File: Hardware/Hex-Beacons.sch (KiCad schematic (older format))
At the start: 0 parts

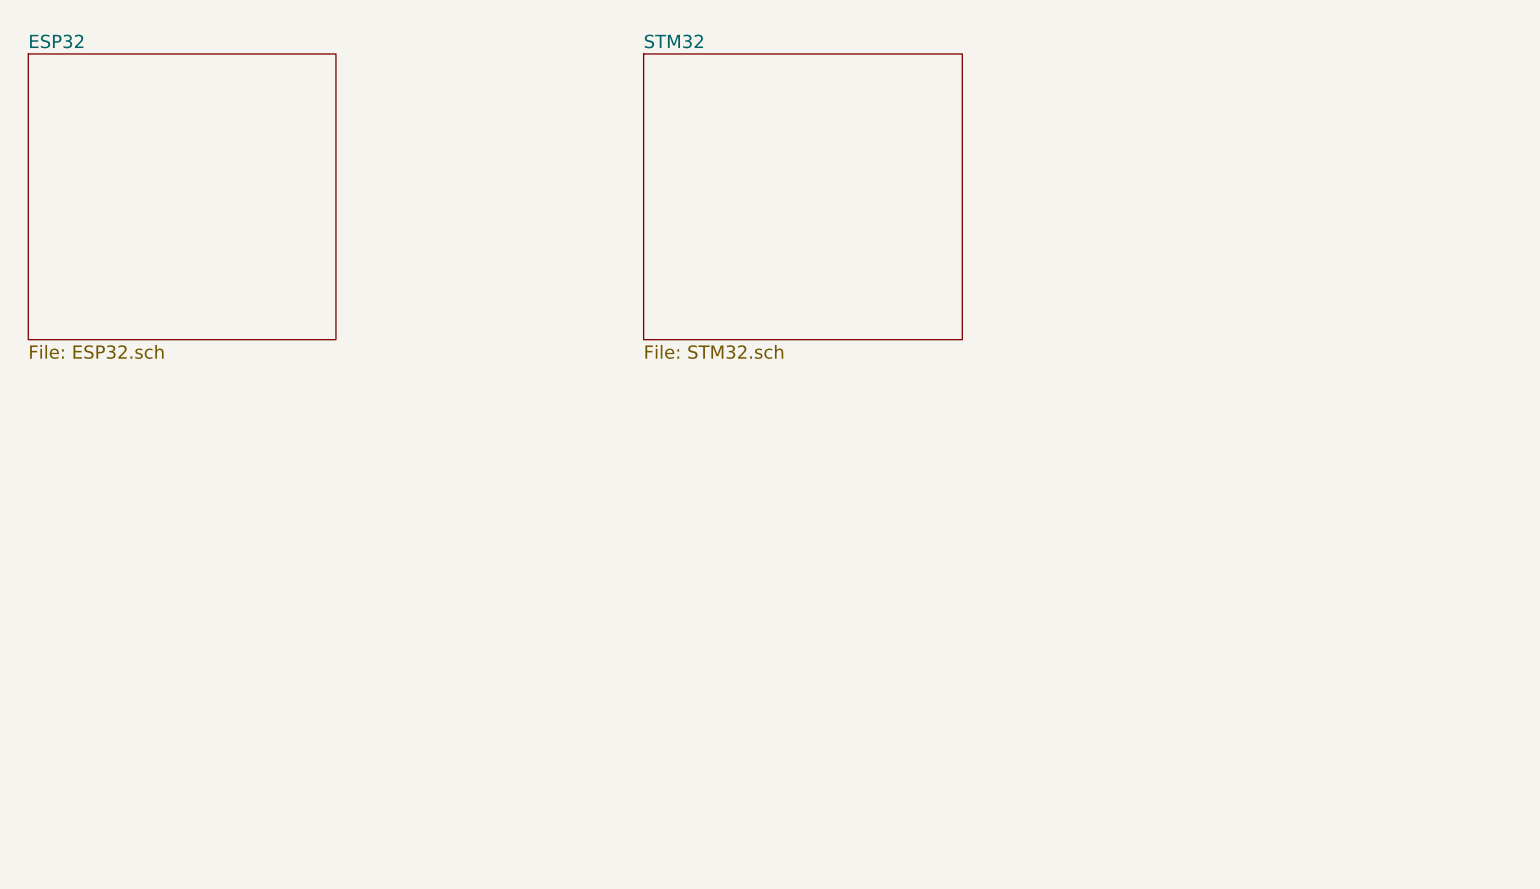
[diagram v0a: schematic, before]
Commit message: Base ESP32 sheet done. STM32 in place
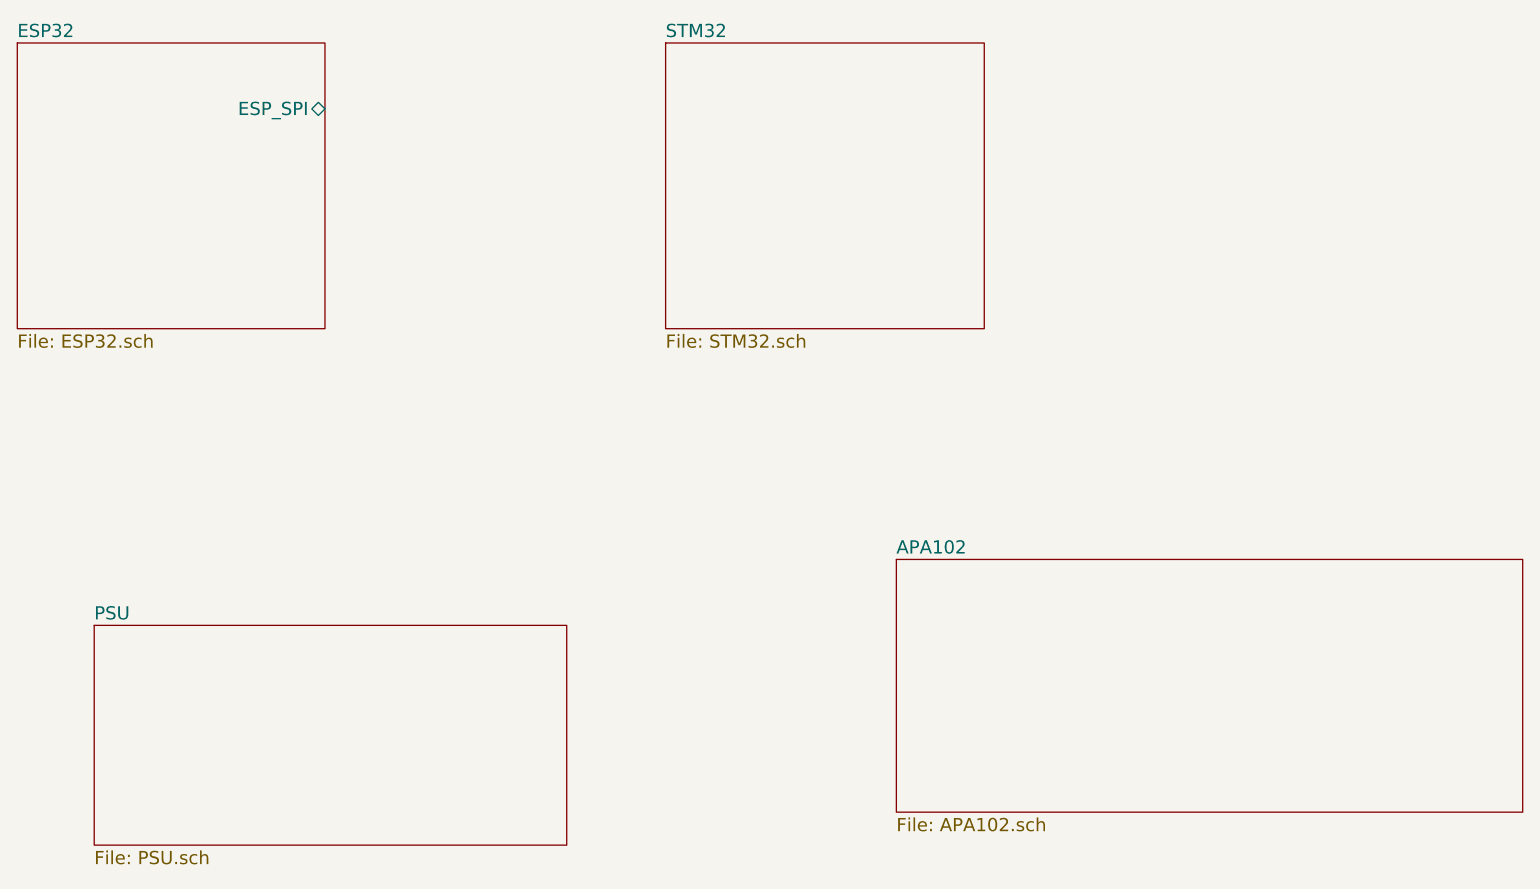
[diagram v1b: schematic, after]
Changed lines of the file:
@@
 LIBS:contrib
 LIBS:valves
-LIBS:crumpschemes
-LIBS:ESP32-footprints-Shem-Lib
-LIBS:espressif-xess
-LIBS:74xgxx
-LIBS:ac-dc
-LIBS:actel
-LIBS:allegro
-LIBS:Altera
-LIBS:analog_devices
-LIBS:battery_management
-LIBS:bbd
-LIBS:bosch
-LIBS:brooktre
-LIBS:cmos_ieee
-LIBS:dc-dc
-LIBS:diode
-LIBS:elec-unifil
-LIBS:ESD_Protection
-LIBS:ftdi
-LIBS:gennum
-LIBS:graphic
-LIBS:hc11
-LIBS:ir
-LIBS:Lattice
-LIBS:leds
-LIBS:logo
-LIBS:maxim
-LIBS:mechanical
-LIBS:microchip_dspic33dsc
-LIBS:microchip_pic10mcu
-LIBS:microchip_pic12mcu
-LIBS:microchip_pic16mcu
-LIBS:microchip_pic18mcu
-LIBS:microchip_pic24mcu
-LIBS:microchip_pic32mcu
-LIBS:modules
-LIBS:motor_drivers
-LIBS:motors
-LIBS:msp430
-LIBS:nordicsemi
-LIBS:nxp
-LIBS:nxp_armmcu
-LIBS:onsemi
-LIBS:Oscillators
-LIBS:Power_Management
-LIBS:powerint
-LIBS:pspice
-LIBS:references
-LIBS:relays
-LIBS:rfcom
-LIBS:sensors
-LIBS:silabs
-LIBS:stm8
-LIBS:stm32
-LIBS:supertex
-LIBS:switches
-LIBS:transf
-LIBS:triac_thyristor
-LIBS:ttl_ieee
-LIBS:video
-LIBS:wiznet
-LIBS:Worldsemi
-LIBS:Xicor
-LIBS:zetex
-LIBS:Zilog
-LIBS:Beacons-cache
+LIBS:STM32F042C6T6
+LIBS:Hex-Beacons-cache
 EELAYER 25 0
 EELAYER END
 $Descr A4 11693 8268
 encoding utf-8
-Sheet 1 3
+Sheet 1 5
 Title ""
 Date ""
@@
 $EndDescr
 $Sheet
-S 3050 2350 1400 1300
+S 3000 2300 1400 1300
 U 59AC571E
 F0 "ESP32" 60
 F1 "ESP32.sch" 60
+F2 "ESP_SPI" B R 4400 2600 60
 $EndSheet
 $Sheet
-S 5850 2350 1450 1300
+S 5950 2300 1450 1300
 U 59AC5A80
 F0 "STM32" 60
 F1 "STM32.sch" 60
 $EndSheet
+$Sheet
+S 3350 4950 2150 1000
+U 59ADA955
+F0 "PSU" 60
+F1 "PSU.sch" 60
+$EndSheet
+$Sheet
+S 7000 4650 2850 1150
+U 59ADAAF7
+F0 "APA102" 60
+F1 "APA102.sch" 60
+$EndSheet
 $EndSCHEMATC
